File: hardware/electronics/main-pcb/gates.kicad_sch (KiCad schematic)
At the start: 39 parts, among them IC14 LM5109BSDX_NOPB, IC15 LM5109BSDX_NOPB, IC16 LM5109BSDX_NOPB, IC17 LM5109BSDX_NOPB, IC18 INA2181A2IDGSR, Q22 30V 71A, Q23 30V 71A, Q24 30V 71A, Q25 30V 71A, Q26 30V 71A, Q27 30V 71A, Q28 30V 71A

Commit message: worked on cmsis dap implementation aswell as cleaned up startup files for both microcontrolers
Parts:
- renumbered D76 to D77, D77 to D78, D78 to D79, D79 to D80, R103 to R105, R104 to R106, R105 to R107, R106 to R108, R107 to R109, R108 to R110, R109 to R111, R110 to R112, R111 to R113, R112 to R114, R113 to R115, R114 to R116, R115 to R117, R116 to R118

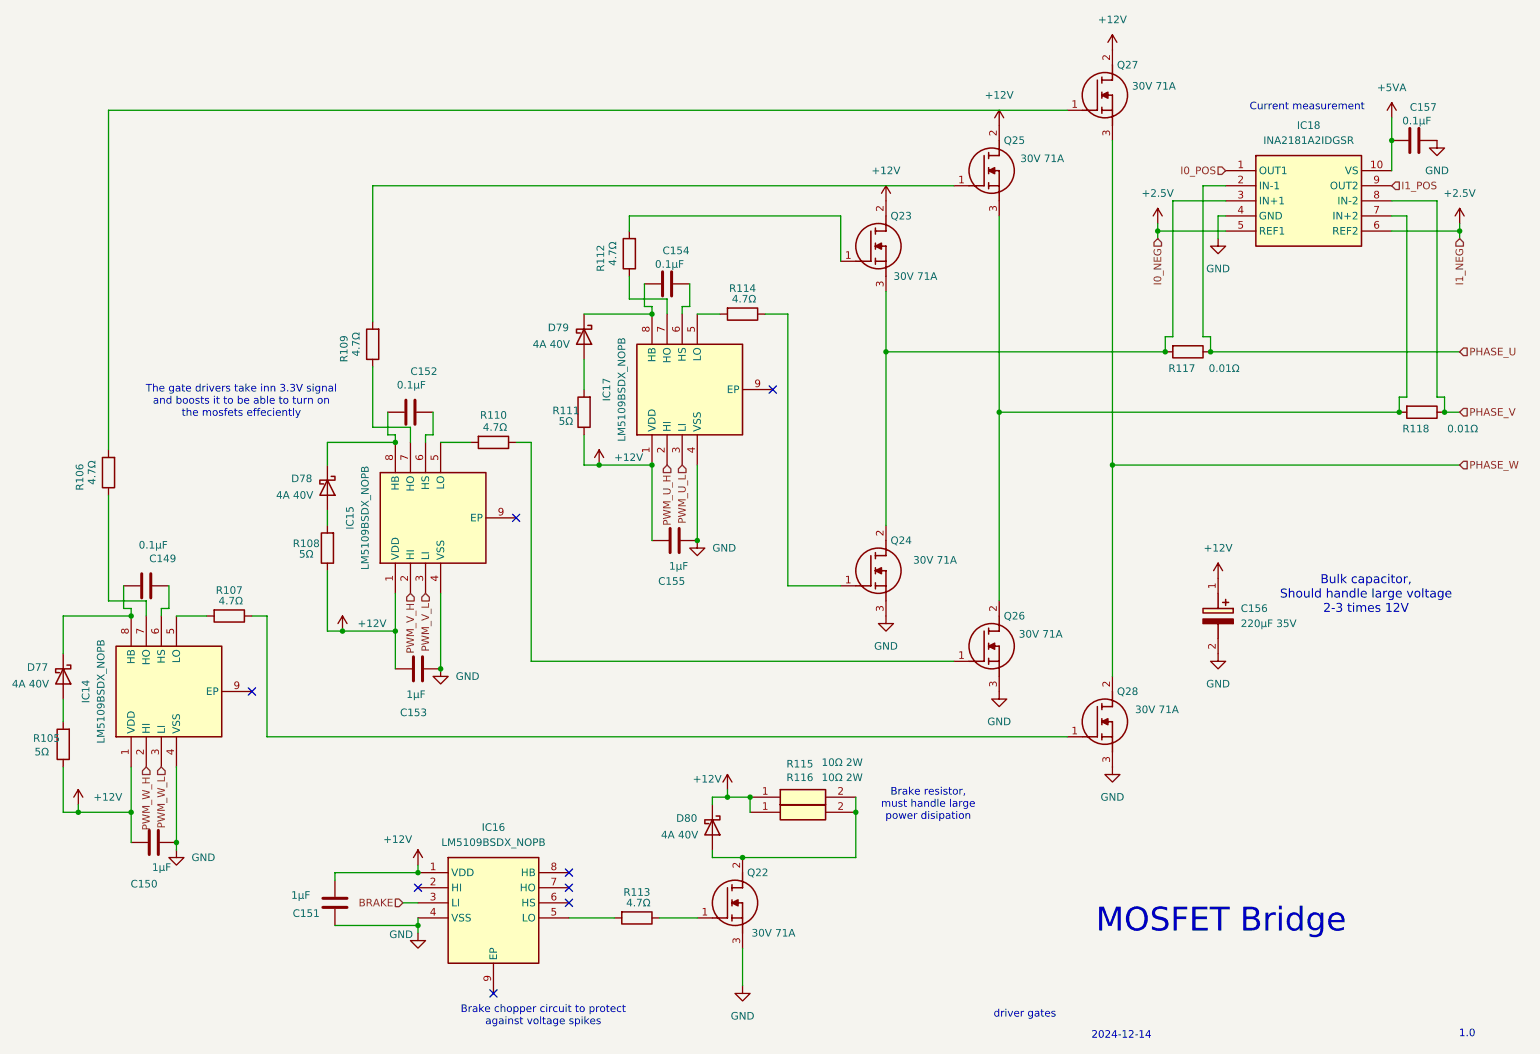
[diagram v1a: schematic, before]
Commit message: added bom
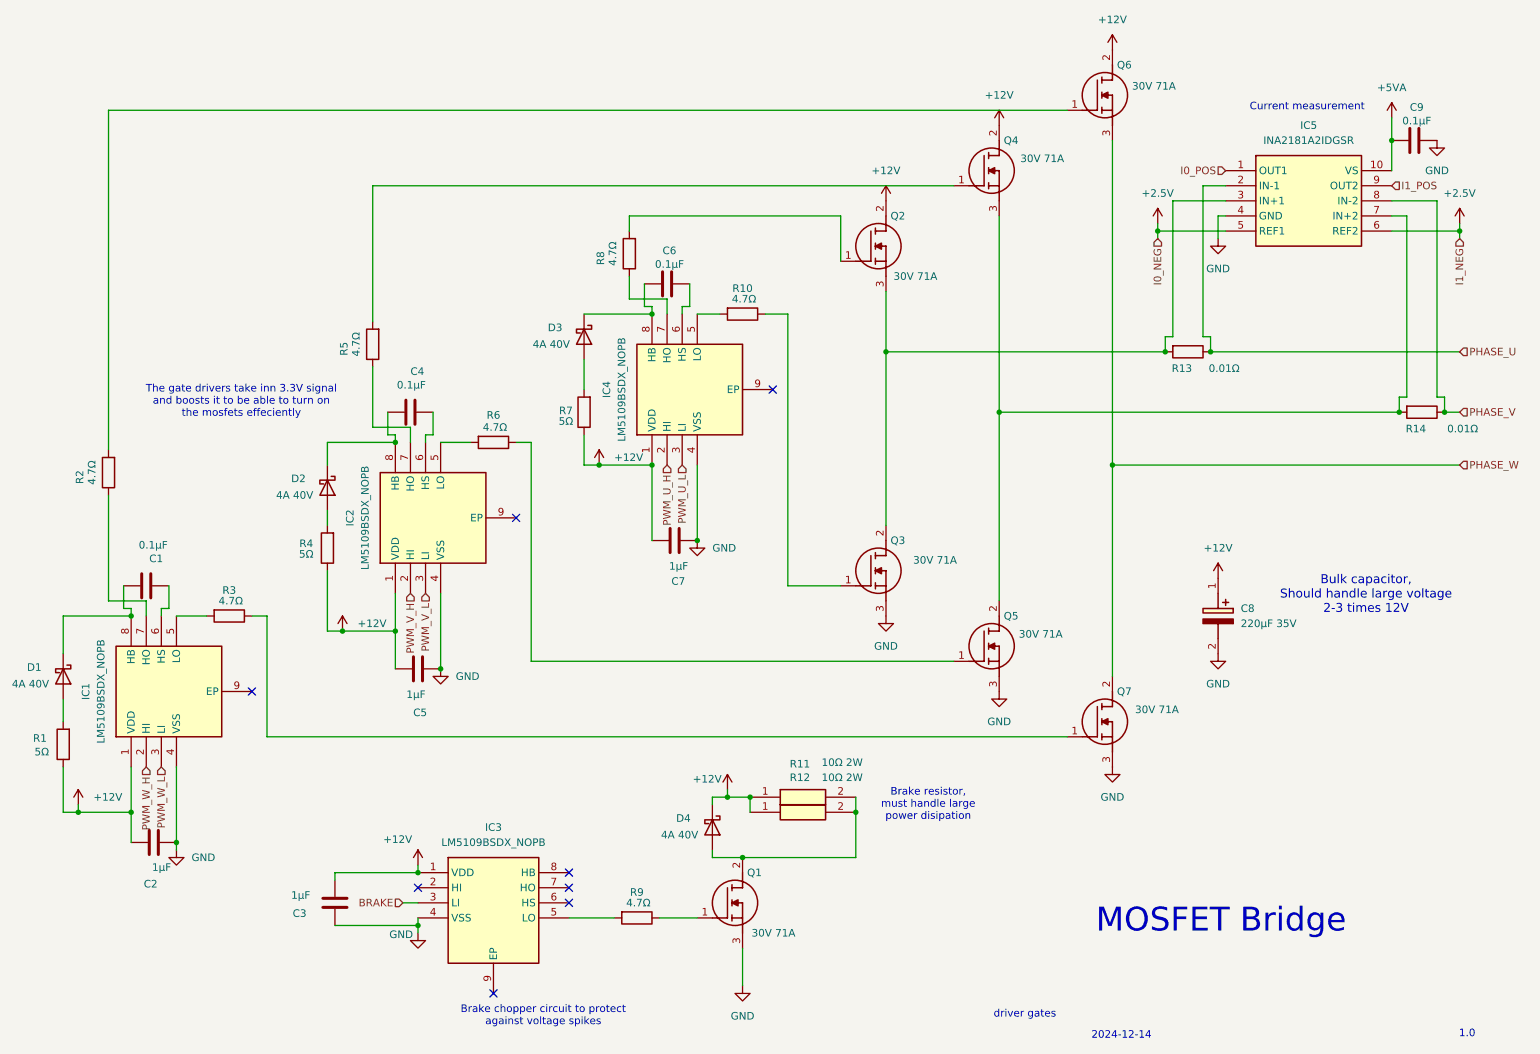
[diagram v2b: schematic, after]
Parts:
- renumbered C149 to C1, C150 to C2, C151 to C3, C152 to C4, C153 to C5, C154 to C6, C155 to C7, C156 to C8, C157 to C9, D77 to D1, D78 to D2, D79 to D3, D80 to D4, IC14 to IC1, IC15 to IC2, IC16 to IC3, IC17 to IC4, IC18 to IC5, Q22 to Q1, Q23 to Q2, Q24 to Q3, Q25 to Q4, Q26 to Q5, Q27 to Q6, Q28 to Q7, R105 to R1, R114 to R10, R115 to R11, R116 to R12, R117 to R13, R118 to R14, R106 to R2, R107 to R3, R108 to R4, R109 to R5, R110 to R6, R111 to R7, R112 to R8, R113 to R9
